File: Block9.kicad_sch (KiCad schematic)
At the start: 2 parts, among them SW3 SW_Push

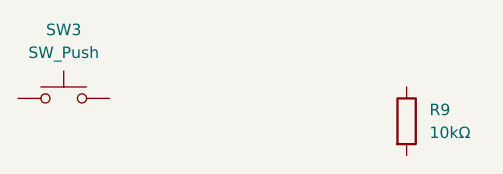
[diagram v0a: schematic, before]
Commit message: Adding NXP modules
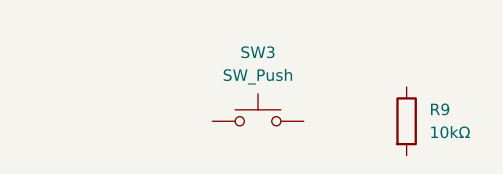
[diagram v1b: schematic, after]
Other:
- moved on the sheet: SW3
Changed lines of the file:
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@@
 	(symbol
 		(lib_id "Switch:SW_Push")
-		(at 83.82 104.14 0)
+		(at 105.41 106.68 0)
 		(unit 1)
 		(body_style 1)
@@
 		(fields_autoplaced yes)
 		(property "Reference" "SW3"
-			(at 83.82 96.52 0)
+			(at 105.41 99.06 0)
 			(show_name no)
 			(do_not_autoplace no)
@@
 		)
 		(property "Value" "SW_Push"
-			(at 83.82 99.06 0)
+			(at 105.41 101.6 0)
 			(show_name no)
 			(do_not_autoplace no)
@@
 		)
 		(property "Footprint" "Button_Switch_SMD:SW_SPST_TL3305A"
-			(at 83.82 99.06 0)
+			(at 105.41 101.6 0)
 			(hide yes)
 			(show_name no)
@@
 		)
 		(property "Datasheet" ""
-			(at 83.82 99.06 0)
+			(at 105.41 101.6 0)
 			(hide yes)
 			(show_name no)
@@
 		)
 		(property "Description" "Push button switch, generic, two pins"
-			(at 83.82 104.14 0)
+			(at 105.41 106.68 0)
 			(hide yes)
 			(show_name no)
